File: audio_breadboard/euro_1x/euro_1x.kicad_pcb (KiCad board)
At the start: 2 copper layers, 182.9 x 87.6 mm, 32 parts, among them J1 EURO POWER, J10 IN, J11 IN, J12 OUT, J13 OUT, J14 AUX1, J15 AUX2, J16 Jumper, J17 Jumper, J18 GND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

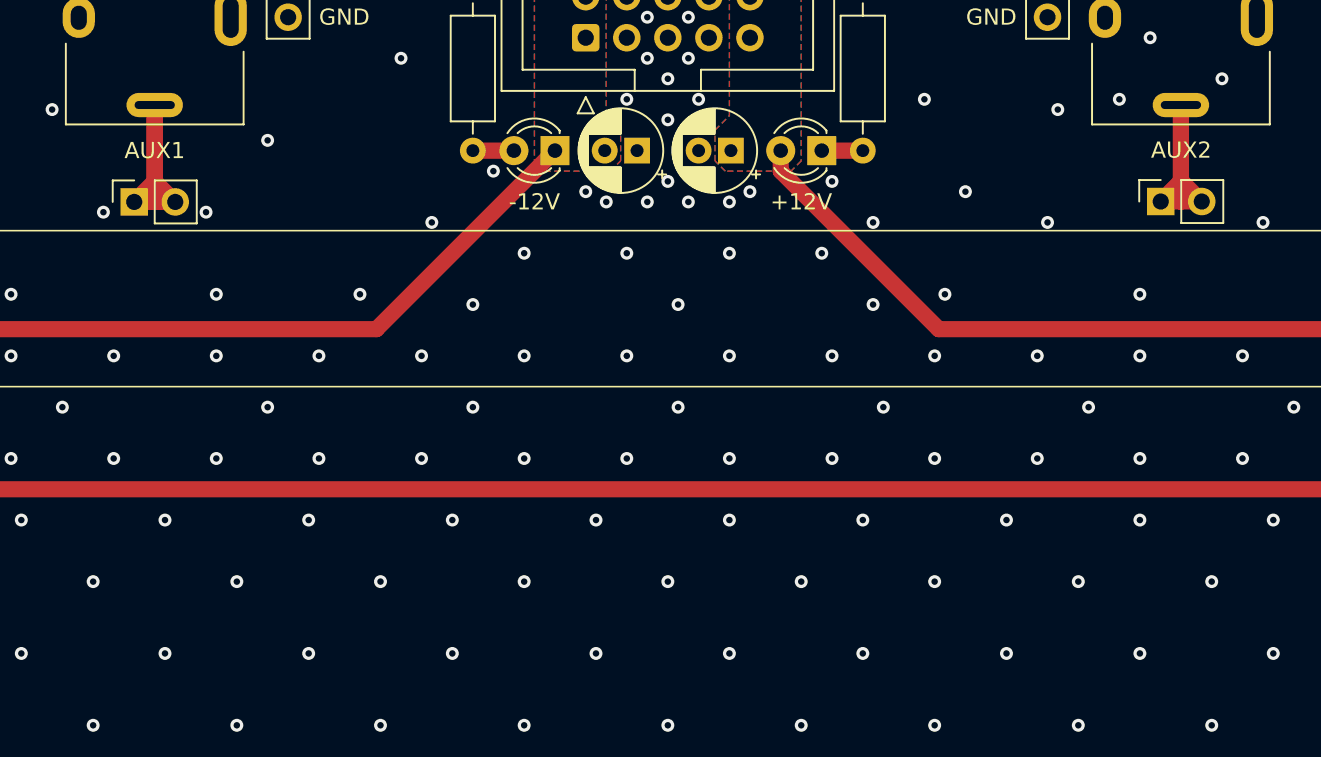
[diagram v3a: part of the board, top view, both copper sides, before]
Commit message: Finalize board layouts
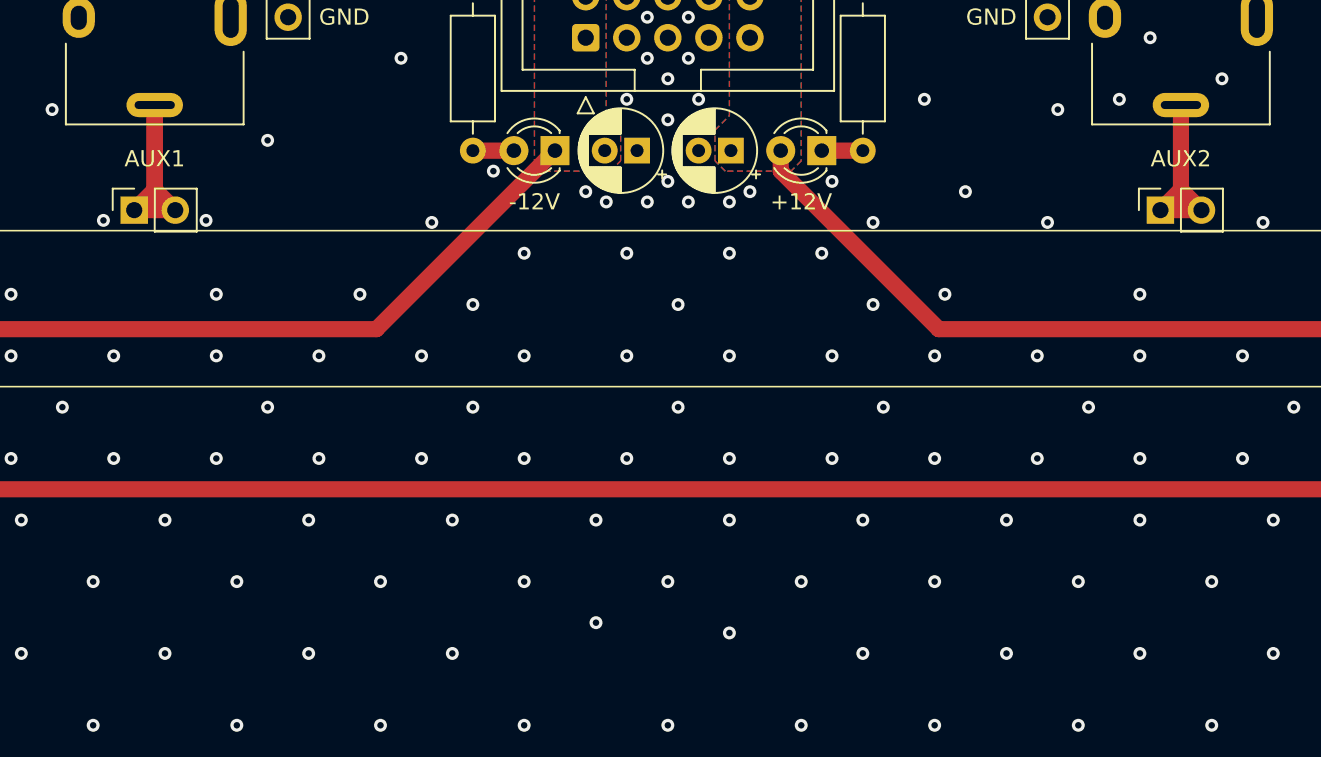
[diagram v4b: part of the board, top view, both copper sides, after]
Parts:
- moved J15 0.53 mm to (182.9, 72.9)
- moved J14 0.51 mm to (119.4, 72.9)
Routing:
- net /1x Breadboard (Eurorack Power)/AUX2: track 16.8 -> 12.1 mm
- net /1x Breadboard (Eurorack Power)/AUX1: track 16.9 -> 18.6 mm
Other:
- board text added: "Audio Breadboard 1x Max Proskauer Jan 2024 v0.1 github.com/mprosk/audio_breadboard"
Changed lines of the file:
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@@
       (drillshape 0)
       (scaleselection 1)
-      (outputdirectory "../gerber/euro_1x/")
+      (outputdirectory "../../gerber/euro_1x")
     )
   )
@@
   )
   (footprint "Connector_PinSocket_2.54mm:PinSocket_1x02_P2.54mm_Vertical" (layer "F.Cu")
-    (at 119.38 72.39 90)
+    (at 119.38 72.898 90)
     (descr "Through hole straight socket strip, 1x02, 2.54mm pitch, single row (from Kicad 4.0.7), script generated")
     (tags "Through hole socket strip THT 1x02 2.54mm single row")
@@
   )
   (footprint "Connector_PinSocket_2.54mm:PinSocket_1x02_P2.54mm_Vertical" (layer "F.Cu")
-    (at 182.9 72.365 90)
+    (at 182.88 72.898 90)
     (descr "Through hole straight socket strip, 1x02, 2.54mm pitch, single row (from Kicad 4.0.7), script generated")
     (tags "Through hole socket strip THT 1x02 2.54mm single row")
@@
     (effects (font (size 1.5 1.5) (thickness 0.25)) (justify mirror))
   )
+  (gr_text "Audio Breadboard 1x\nMax Proskauer  Jan 2024  v0.1\ngithub.com/mprosk/audio_breadboard" (at 152.4 101.6) (layer "B.SilkS")
+    (effects (font (size 1 1) (thickness 0.15)) (justify mirror))
+  )
   (gr_text "GND" (at 86.36 60.96) (layer "F.SilkS")
     (effects (font (size 1 1) (thickness 0.15)) (justify left))
@@
   (via (at 107.95 95.885) (size 0.8) (drill 0.4) (layers "F.Cu" "B.Cu") (free) (net 2))
   (via (at 189.865 100.33) (size 0.8) (drill 0.4) (layers "F.Cu" "B.Cu") (free) (net 2))
-  (via (at 123.825 73.025) (size 0.8) (drill 0.4) (layers "F.Cu" "B.Cu") (free) (net 2))
+  (via (at 123.825 73.533) (size 0.8) (drill 0.4) (layers "F.Cu" "B.Cu") (free) (net 2))
   (via (at 103.505 120.65) (size 0.8) (drill 0.4) (layers "F.Cu" "B.Cu") (free) (net 2))
   (via (at 94.615 92.075) (size 0.8) (drill 0.4) (layers "F.Cu" "B.Cu") (free) (net 2))
@@
   (via (at 160.655 116.205) (size 0.8) (drill 0.4) (layers "F.Cu" "B.Cu") (free) (net 2))
   (via (at 203.2 95.885) (size 0.8) (drill 0.4) (layers "F.Cu" "B.Cu") (free) (net 2))
-  (via (at 156.21 100.33) (size 0.8) (drill 0.4) (layers "F.Cu" "B.Cu") (free) (net 2))
+  (via (at 156.21 99.06) (size 0.8) (drill 0.4) (layers "F.Cu" "B.Cu") (free) (net 2))
   (via (at 207.01 128.905) (size 0.8) (drill 0.4) (layers "F.Cu" "B.Cu") (free) (net 2))
   (via (at 151.13 58.42) (size 0.8) (drill 0.4) (layers "F.Cu" "B.Cu") (free) (net 2))
@@
   (via (at 70.485 85.09) (size 0.8) (drill 0.4) (layers "F.Cu" "B.Cu") (free) (net 2))
   (via (at 111.76 81.915) (size 0.8) (drill 0.4) (layers "F.Cu" "B.Cu") (free) (net 2))
-  (via (at 117.475 73.025) (size 0.8) (drill 0.4) (layers "F.Cu" "B.Cu") (free) (net 2))
+  (via (at 117.475 73.533) (size 0.8) (drill 0.4) (layers "F.Cu" "B.Cu") (free) (net 2))
   (via (at 134.62 104.775) (size 0.8) (drill 0.4) (layers "F.Cu" "B.Cu") (free) (net 2))
   (via (at 147.955 92.075) (size 0.8) (drill 0.4) (layers "F.Cu" "B.Cu") (free) (net 2))
@@
   (via (at 139.065 92.075) (size 0.8) (drill 0.4) (layers "F.Cu" "B.Cu") (free) (net 2))
   (via (at 94.615 108.585) (size 0.8) (drill 0.4) (layers "F.Cu" "B.Cu") (free) (net 2))
-  (via (at 147.955 100.33) (size 0.8) (drill 0.4) (layers "F.Cu" "B.Cu") (free) (net 2))
+  (via (at 147.955 98.425) (size 0.8) (drill 0.4) (layers "F.Cu" "B.Cu") (free) (net 2))
   (via (at 85.725 100.33) (size 0.8) (drill 0.4) (layers "F.Cu" "B.Cu") (free) (net 2))
   (via (at 165.735 85.09) (size 0.8) (drill 0.4) (layers "F.Cu" "B.Cu") (free) (net 2))
@@
   (segment (start 228.6 58.295) (end 220.47 58.295) (width 1) (layer "F.Cu") (net 6))
   (segment (start 220.47 58.295) (end 220.345 58.42) (width 1) (layer "F.Cu") (net 6))
-  (segment (start 119.38 72.39) (end 120.65 72.39) (width 1) (layer "F.Cu") (net 7))
-  (segment (start 121.92 72.39) (end 120.65 71.12) (width 1) (layer "F.Cu") (net 7))
-  (segment (start 120.65 66.395) (end 120.65 71.12) (width 1) (layer "F.Cu") (net 7))
-  (segment (start 120.65 71.12) (end 119.38 72.39) (width 1) (layer "F.Cu") (net 7))
+  (segment (start 119.38 72.898) (end 120.65 72.898) (width 1) (layer "F.Cu") (net 7))
+  (segment (start 120.65 66.395) (end 120.65 72.898) (width 1) (layer "F.Cu") (net 7))
+  (segment (start 121.92 72.898) (end 120.65 71.628) (width 1) (layer "F.Cu") (net 7))
+  (segment (start 120.65 71.628) (end 119.38 72.898) (width 1) (layer "F.Cu") (net 7))
   (segment (start 120.65 66.395) (end 120.65 72.39) (width 1) (layer "F.Cu") (net 7))
-  (segment (start 120.65 72.39) (end 121.92 72.39) (width 1) (layer "F.Cu") (net 7))
+  (segment (start 120.65 72.898) (end 121.92 72.898) (width 1) (layer "F.Cu") (net 7))
   (segment (start 128.78 58.295) (end 128.905 58.42) (width 1) (layer "F.Cu") (net 8))
   (segment (start 120.65 58.295) (end 128.78 58.295) (width 1) (layer "F.Cu") (net 8))
-  (segment (start 184.15 71.115) (end 182.9 72.365) (width 1) (layer "F.Cu") (net 9))
-  (segment (start 184.19 71.115) (end 184.15 71.115) (width 1) (layer "F.Cu") (net 9))
-  (segment (start 185.44 72.365) (end 184.19 71.115) (width 1) (layer "F.Cu") (net 9))
-  (segment (start 185.44 72.365) (end 184.15 72.365) (width 1) (layer "F.Cu") (net 9))
+  (segment (start 184.13 71.648) (end 182.88 72.898) (width 1) (layer "F.Cu") (net 9))
+  (segment (start 184.17 71.648) (end 184.13 71.648) (width 1) (layer "F.Cu") (net 9))
+  (segment (start 185.42 72.898) (end 184.17 71.648) (width 1) (layer "F.Cu") (net 9))
+  (segment (start 185.42 72.898) (end 184.13 72.898) (width 1) (layer "F.Cu") (net 9))
   (segment (start 184.15 66.395) (end 184.15 72.365) (width 1) (layer "F.Cu") (net 9))
-  (segment (start 184.15 72.365) (end 182.9 72.365) (width 1) (layer "F.Cu") (net 9))
-  (segment (start 184.15 66.395) (end 184.15 71.115) (width 1) (layer "F.Cu") (net 9))
+  (segment (start 184.13 72.898) (end 182.88 72.898) (width 1) (layer "F.Cu") (net 9))
   (segment (start 184.15 58.295) (end 176.02 58.295) (width 1) (layer "F.Cu") (net 10))
   (segment (start 176.02 58.295) (end 175.895 58.42) (width 1) (layer "F.Cu") (net 10))
